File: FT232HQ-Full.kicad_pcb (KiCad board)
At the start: 4 copper layers, 27.9 x 24.1 mm, 29 parts, among them J1 USB_C_Receptacle_USB2.0_16P, J2 Conn_02x10_Odd_Even, J3 Conn_01x01, U4 12M, U5 FT232H, U6 93LCxxBxxOT

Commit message: update
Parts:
- J3: footprint 1st_commonly:hole -> 1st_commonly:NUT_SMD_M2.5_4.5_3.0
- turned L2 to 180 degrees
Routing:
- net +3V3: track 12.3 -> 44.7 mm
- net +5V: track 9.27 -> 41.2 mm, vias 5 -> 4
- net GND: track 7.88 -> 6.26 mm, vias 17 -> 12
- net /VPHY: track 3.94 -> 4.59 mm
- removed copper zone on In2.Cu, net +3V3
- removed copper zone on In1.Cu, net +5V
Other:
- copper layers 4 -> 2

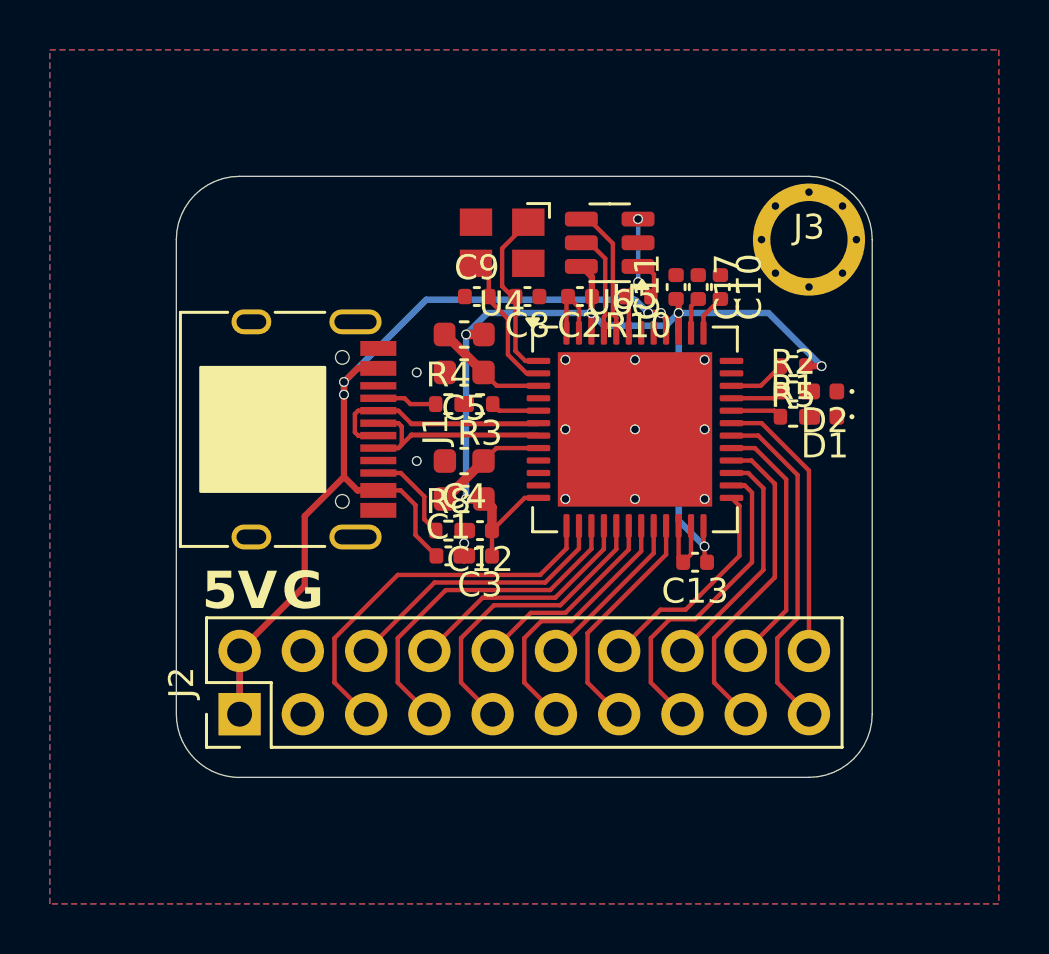
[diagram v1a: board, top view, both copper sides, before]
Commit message: add raspberrypi jst-sh1.0 uart
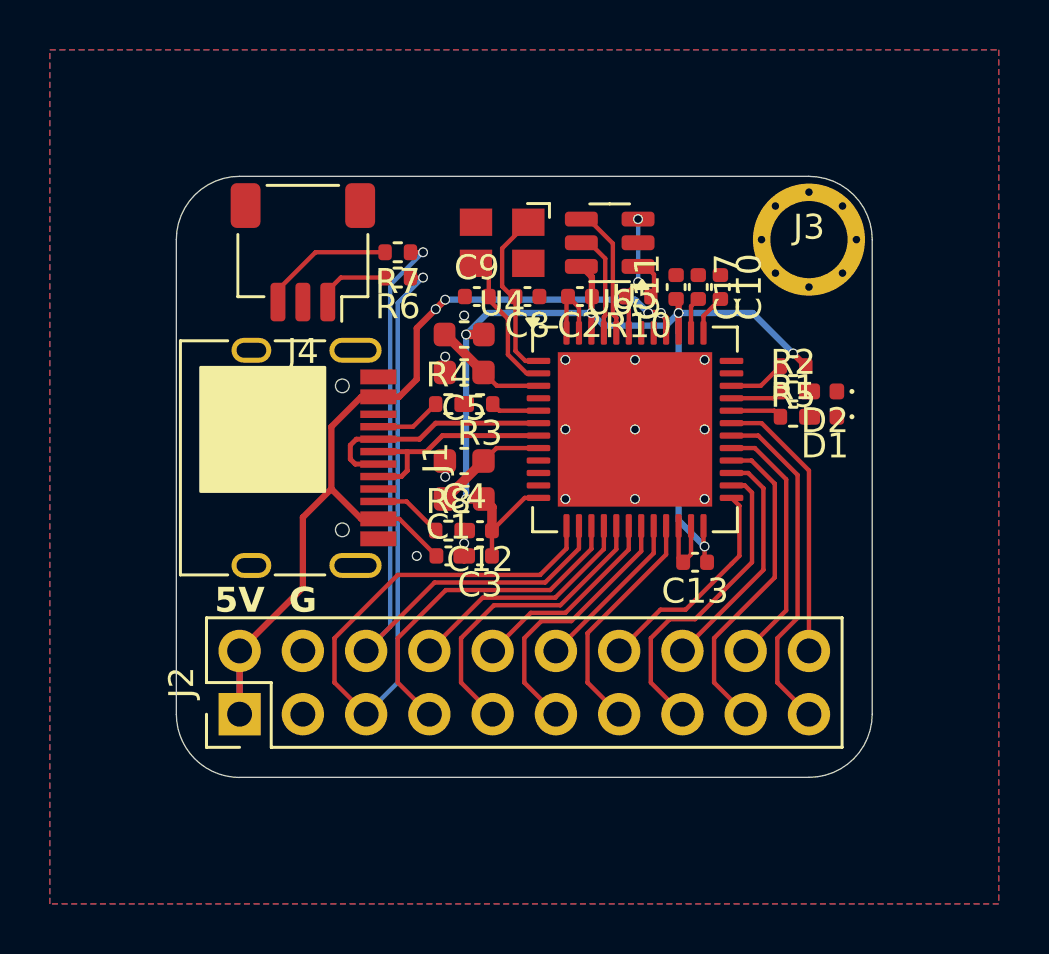
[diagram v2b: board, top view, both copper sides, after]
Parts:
- added J4: Conn_01x03_MountingPin, Connector_JST:JST_SH_SM03B-SRSS-TB_1x03-1MP_P1.00mm_Horizontal, F.Cu at (124.4, 68.9)
- added R6: 100, Resistor_SMD:R_0402_1005Metric, F.Cu at (128.2, 69.9)
- added R7: 100, Resistor_SMD:R_0402_1005Metric, F.Cu at (128.2, 68.9)
- moved J1 1.14 mm to (123.4, 77.2)
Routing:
- net /AD0: track 15.3 -> 34.3 mm, vias 0 -> 1
- net /AD1: track 11.2 -> 28.6 mm, vias 0 -> 1
- net /RX: track 0.00 -> 4.92 mm
- net /TX: track 0.00 -> 2.52 mm
- net +3V3: track 44.7 -> 43.4 mm
- net /CC2: track 3.80 -> 2.79 mm
- net +5V: track 41.2 -> 40.2 mm
- net GND: vias 12 -> 14

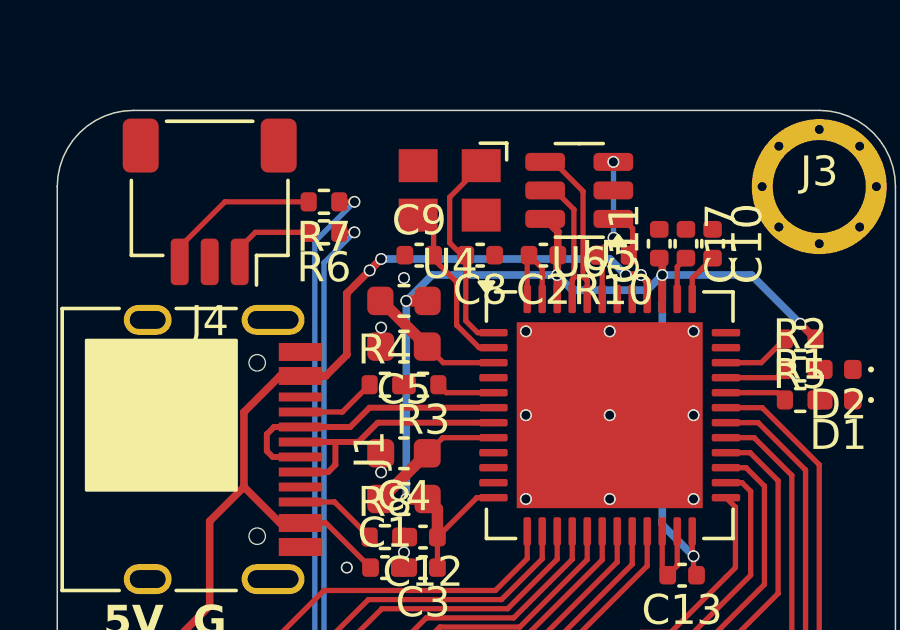
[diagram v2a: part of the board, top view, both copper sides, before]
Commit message: add 2.2uf to 5v
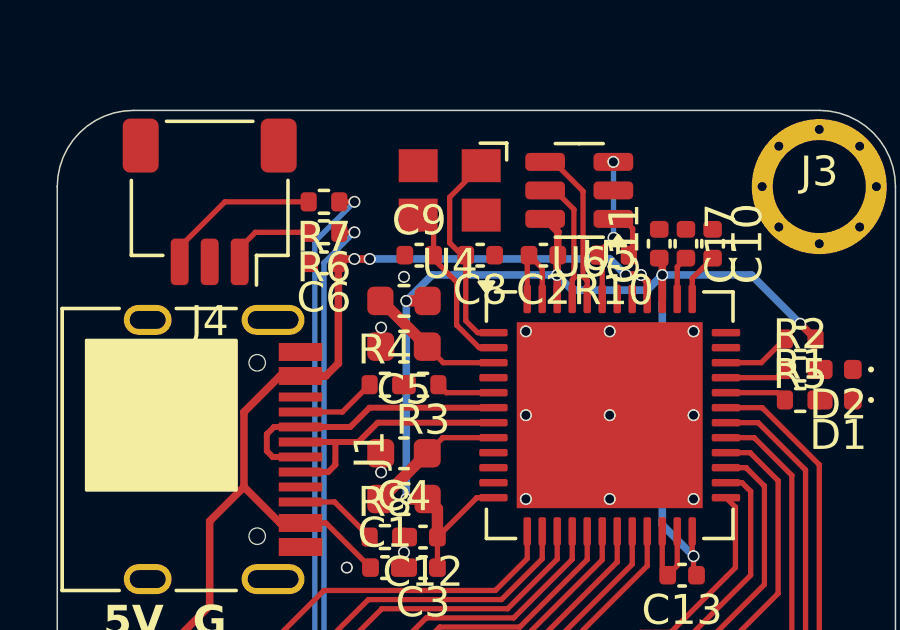
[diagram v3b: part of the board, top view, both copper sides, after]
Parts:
- added C6: 225, Capacitor_SMD:C_0402_1005Metric, F.Cu at (128.2, 70.9)
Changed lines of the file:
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@@
 		(tags "resistor")
 		(property "Reference" "R7"
-			(at 0 -1.17 360)
+			(at 0 -1.17 0)
 			(layer "F.SilkS")
 			(effects
@@
 		)
 		(property "Value" "100"
-			(at 0 1.17 360)
+			(at 0 1.17 0)
 			(layer "F.Fab")
 			(effects
@@
 		)
 		(fp_text user "${REFERENCE}"
-			(at 0 0 360)
+			(at 0 0 0)
 			(layer "F.Fab")
 			(effects
@@
 		(tags "connector JST SH horizontal")
 		(property "Reference" "J4"
-			(at 0 -3.98 360)
+			(at 0 -3.98 0)
 			(layer "F.SilkS")
 			(effects
@@
 		)
 		(property "Value" "Conn_01x03_MountingPin"
-			(at 0 3.98 360)
+			(at 0 3.98 0)
 			(layer "F.Fab")
 			(effects
@@
 		)
 		(fp_text user "${REFERENCE}"
-			(at 0 0 360)
+			(at 0 0 0)
 			(layer "F.Fab")
 			(effects
@@
 	(footprint "Capacitor_SMD:C_0402_1005Metric"
 		(layer "F.Cu")
+		(at 128.202 70.928 180)
+		(descr "Capacitor SMD 0402 (1005 Metric), square (rectangular) end terminal, IPC_7351 nominal, (Body size source: IPC-SM-782 page 76, https://www.pcb-3d.com/wordpress/wp-content/uploads/ipc-sm-782a_amendment_1_and_2.pdf), generated with kicad-footprint-generator")
+		(tags "capacitor")
+		(property "Reference" "C6"
+			(at 0 -1.16 360)
+			(layer "F.SilkS")
+			(effects
+				(font
+					(size 1 1)
+					(thickness 0.15)
+				)
+			)
+		)
+		(property "Value" "225"
+			(at 0 1.16 360)
+			(layer "F.Fab")
+			(effects
+				(font
+					(size 1 1)
+					(thickness 0.15)
+				)
+			)
+		)
+		(property "Footprint" "Capacitor_SMD:C_0402_1005Metric"
+			(at 0 0 180)
+			(unlocked yes)
+			(layer "F.Fab")
+			(hide yes)
+			(effects
+				(font
+					(size 1.27 1.27)
+					(thickness 0.15)
+				)
+			)
+		)
+		(property "Datasheet" ""
+			(at 0 0 180)
+			(unlocked yes)
+			(layer "F.Fab")
+			(hide yes)
+			(effects
+				(font
+					(size 1.27 1.27)
+					(thickness 0.15)
+				)
+			)
+		)
+		(property "Description" "Unpolarized capacitor"
+			(at 0 0 180)
+			(unlocked yes)
+			(layer "F.Fab")
+			(hide yes)
+			(effects
+				(font
+					(size 1.27 1.27)
+					(thickness 0.15)
+				)
+			)
+		)
+		(property ki_fp_filters "C_*")
+		(sheetname "根目录")
+		(sheetfile "FT232HQ-Full.kicad_sch")
+		(attr smd)
+		(fp_line
+			(start -0.107836 0.36)
+			(end 0.107836 0.36)
+			(stroke
+				(width 0.12)
+				(type solid)
+			)
+			(layer "F.SilkS")
+		)
+		(fp_line
+			(start -0.107836 -0.36)
+			(end 0.107836 -0.36)
+			(stroke
+				(width 0.12)
+				(type solid)
+			)
+			(layer "F.SilkS")
+		)
+		(fp_line
+			(start 0.91 0.46)
+			(end -0.91 0.46)
+			(stroke
+				(width 0.05)
+				(type solid)
+			)
+			(layer "F.CrtYd")
+		)
+		(fp_line
+			(start 0.91 -0.46)
+			(end 0.91 0.46)
+			(stroke
+				(width 0.05)
+				(type solid)
+			)
+			(layer "F.CrtYd")
+		)
+		(fp_line
+			(start -0.91 0.46)
+			(end -0.91 -0.46)
+			(stroke
+				(width 0.05)
+				(type solid)
+			)
+			(layer "F.CrtYd")
+		)
+		(fp_line
+			(start -0.91 -0.46)
+			(end 0.91 -0.46)
+			(stroke
+				(width 0.05)
+				(type solid)
+			)
+			(layer "F.CrtYd")
+		)
+		(fp_line
+			(start 0.5 0.25)
+			(end -0.5 0.25)
+			(stroke
+				(width 0.1)
+				(type solid)
+			)
+			(layer "F.Fab")
+		)
+		(fp_line
+			(start 0.5 -0.25)
+			(end 0.5 0.25)
+			(stroke
+				(width 0.1)
+				(type solid)
+			)
+			(layer "F.Fab")
+		)
+		(fp_line
+			(start -0.5 0.25)
+			(end -0.5 -0.25)
+			(stroke
+				(width 0.1)
+				(type solid)
+			)
+			(layer "F.Fab")
+		)
+		(fp_line
+			(start -0.5 -0.25)
+			(end 0.5 -0.25)
+			(stroke
+				(width 0.1)
+				(type solid)
+			)
+			(layer "F.Fab")
+		)
+		(fp_text user "${REFERENCE}"
+			(at 0 0 360)
+			(layer "F.Fab")
+			(effects
+				(font
+					(size 0.25 0.25)
+					(thickness 0.04)
+				)
+			)
+		)
+		(pad "1" smd roundrect
+			(at -0.48 0 180)
+			(size 0.56 0.62)
+			(layers "F.Cu" "F.Paste" "F.Mask")
+			(roundrect_rratio 0.25)
+			(net 1 "+5V")
+			(pintype "passive")
+		)
+		(pad "2" smd roundrect
+			(at 0.48 0 180)
+			(size 0.56 0.62)
+			(layers "F.Cu" "F.Paste" "F.Mask")
+			(roundrect_rratio 0.25)
+			(net 2 "GND")
+			(pintype "passive")
+		)
+		(model "${KICAD8_3DMODEL_DIR}/Capacitor_SMD.3dshapes/C_0402_1005Metric.wrl"
+			(offset
+				(xyz 0 0 0)
+			)
+			(scale
+				(xyz 1 1 1)
+			)
+			(rotate
+				(xyz 0 0 0)
+			)
+		)
+	)
+	(footprint "Capacitor_SMD:C_0402_1005Metric"
+		(layer "F.Cu")
 		(at 131.504 81.088 180)
 		(descr "Capacitor SMD 0402 (1005 Metric), square (rectangular) end terminal, IPC_7351 nominal, (Body size source: IPC-SM-782 page 76, https://www.pcb-3d.com/wordpress/wp-content/uploads/ipc-sm-782a_amendment_1_and_2.pdf), generated with kicad-footprint-generator")
@@
 		(tags "resistor")
 		(property "Reference" "R6"
-			(at 0 -1.17 360)
+			(at 0 -1.17 0)
 			(layer "F.SilkS")
 			(effects
@@
 		)
 		(property "Value" "100"
-			(at 0 1.17 360)
+			(at 0 1.17 0)
 			(layer "F.Fab")
 			(effects
@@
 		)
 		(fp_text user "${REFERENCE}"
-			(at 0 0 360)
+			(at 0 0 0)
 			(layer "F.Fab")
 			(effects
@@
 	)
 	(segment
+		(start 129.218 70.801)
+		(end 128.809 70.801)
+		(width 0.254)
+		(layer "F.Cu")
+		(net 1)
+	)
+	(segment
 		(start 124.392 79.541)
 		(end 125.535 78.398)
@@
 	)
 	(segment
-		(start 127.421 74.701)
-		(end 128.26 74.701)
-		(width 0.254)
-		(layer "F.Cu")
-		(net 1)
-	)
-	(segment
 		(start 138.2604 71.3344)
 		(end 138.7684 71.3344)
@@
 	)
 	(segment
-		(start 128.964 71.944)
-		(end 130.107 70.801)
+		(start 129.218 70.801)
+		(end 129.726 70.801)
 		(width 0.254)
 		(layer "F.Cu")
@@
 	)
 	(segment
-		(start 129.726 71.182)
-		(end 130.107 70.801)
+		(start 128.682 74.279)
+		(end 128.682 70.928)
 		(width 0.254)
 		(layer "F.Cu")
@@
 	)
 	(segment
-		(start 126.738 74.701)
-		(end 127.421 74.701)
+		(start 127.421 74.701)
+		(end 128.26 74.701)
 		(width 0.254)
 		(layer "F.Cu")
@@
 	)
 	(segment
-		(start 138.977 71.543)
-		(end 138.7684 71.3344)
+		(start 128.26 74.701)
+		(end 128.682 74.279)
 		(width 0.254)
 		(layer "F.Cu")
@@
 	)
 	(segment
-		(start 128.964 73.997)
-		(end 128.964 71.944)
+		(start 126.738 74.701)
+		(end 127.421 74.701)
 		(width 0.254)
 		(layer "F.Cu")
@@
 	)
 	(segment
-		(start 128.26 74.701)
-		(end 128.964 73.997)
+		(start 138.977 71.543)
+		(end 138.7684 71.3344)
 		(width 0.254)
 		(layer "F.Cu")
@@
 	)
 	(via
-		(at 129.726 71.182)
+		(at 129.218 70.801)
 		(size 0.4)
 		(drill 0.3)
@@
 	)
 	(via
-		(at 130.107 70.801)
+		(at 129.726 70.801)
 		(size 0.4)
 		(drill 0.3)
@@
 	)
 	(segment
-		(start 130.107 70.801)
+		(start 129.726 70.801)
 		(end 137.727 70.801)
 		(width 0.254)
@@
 	)
 	(segment
-		(start 137.727 70.801)
+		(start 138.7684 71.3344)
 		(end 138.2604 71.3344)
 		(width 0.254)
@@
 	)
 	(segment
-		(start 129.726 71.182)
-		(end 130.107 70.801)
+		(start 137.727 70.801)
+		(end 138.2604 71.3344)
 		(width 0.254)
 		(layer "B.Cu")
@@
 	)
 	(segment
-		(start 138.7684 71.3344)
-		(end 138.2604 71.3344)
+		(start 129.218 70.801)
+		(end 129.726 70.801)
 		(width 0.254)
 		(layer "B.Cu")
@@
 	)
 	(via
-		(at 130.869 71.436)
+		(at 130.869 71.396)
 		(size 0.4)
 		(drill 0.3)
